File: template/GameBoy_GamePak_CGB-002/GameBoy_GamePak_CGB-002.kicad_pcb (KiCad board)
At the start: 2 copper layers, 51 x 60.7 mm, 1 part, among them J1 GameBoy_GamePak_CGB-002

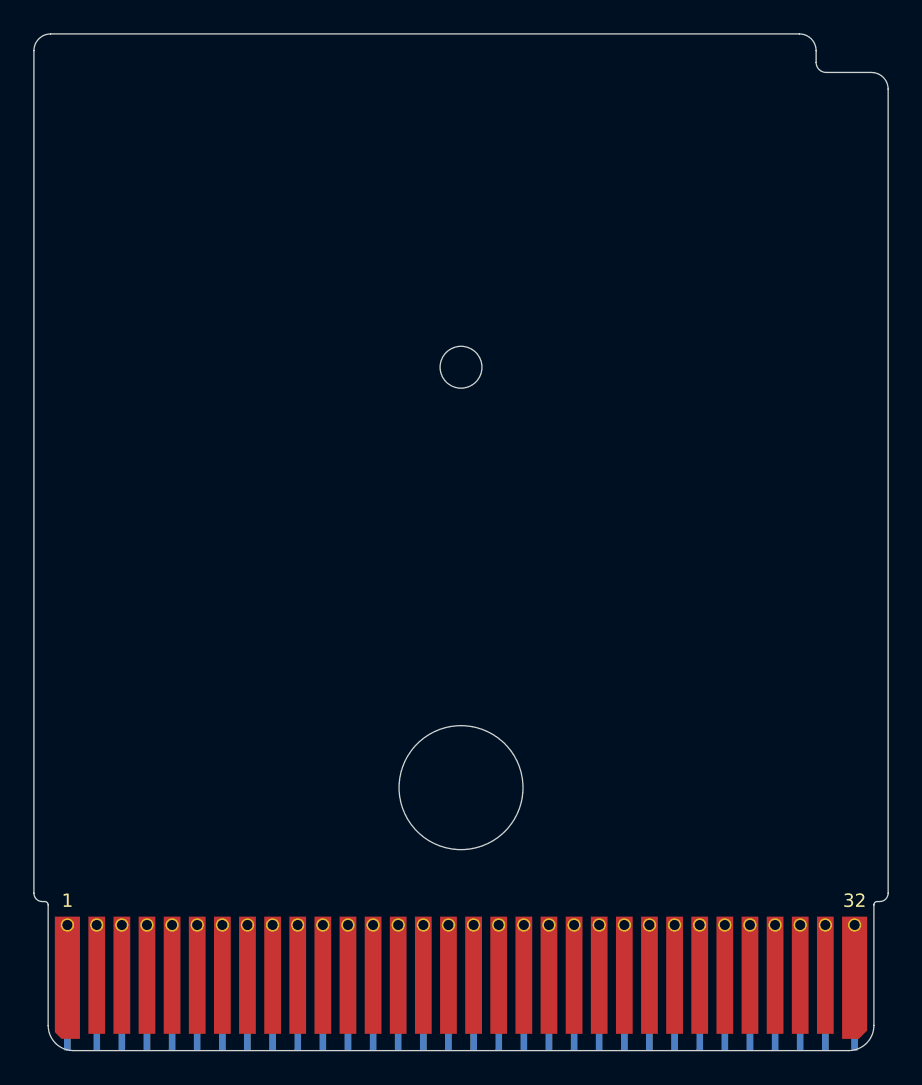
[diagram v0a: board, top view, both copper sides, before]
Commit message: Update all files to KiCAD 6.x format
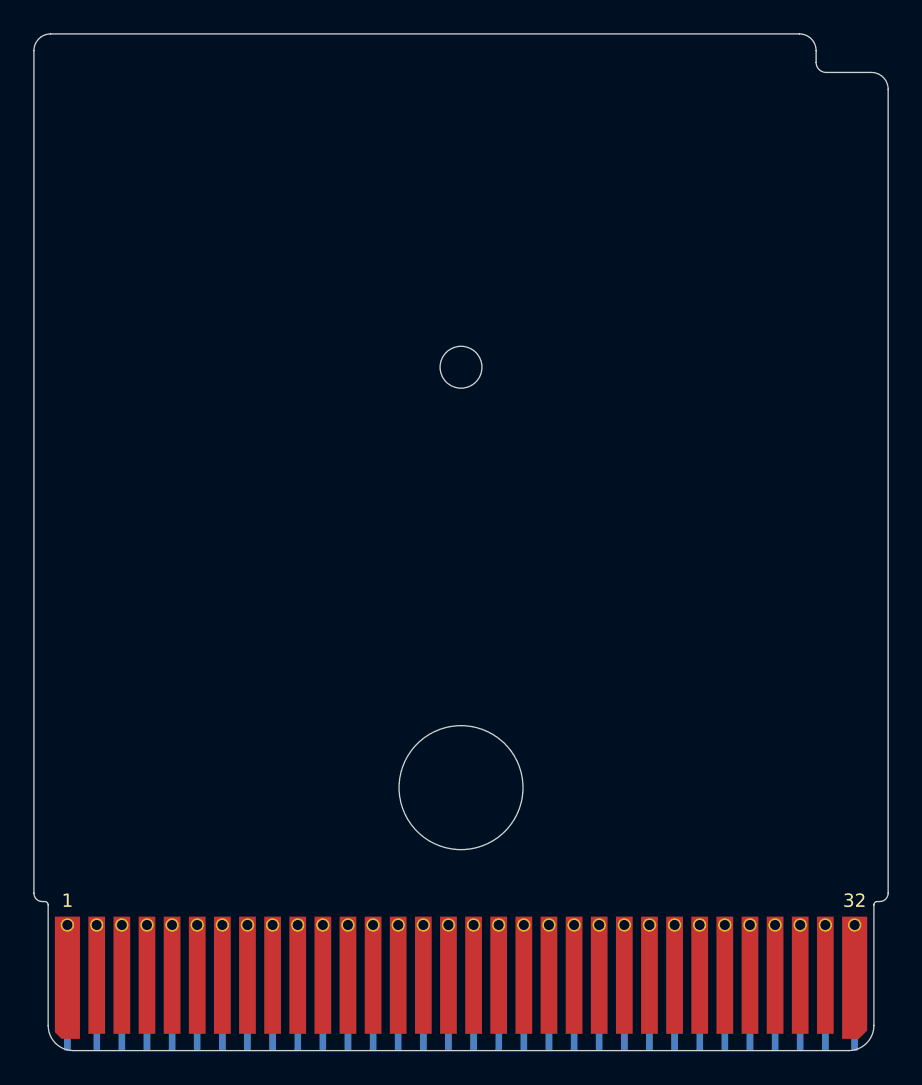
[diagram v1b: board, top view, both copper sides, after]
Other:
- net class Default removed
